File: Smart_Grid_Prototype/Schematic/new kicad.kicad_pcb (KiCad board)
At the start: 2 copper layers, 144.8 x 116.8 mm, 70 parts, among them J1 EXT_POW, J2 24VAC _LOAD, J3 AC_INPUT, J4 DC_LOAD, J5 POW_SHARE, Q1 BD139, Q2 BD139, Q3 BD139, Q4 BD139, Q5 BD139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

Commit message: updated
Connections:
- U1 pad 15: unconnected-(U1-VIN-Pad15) -> /EXT_POWER
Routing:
- net /EXT_POWER: track 114.2 -> 161.9 mm
- net GND: track 452.7 -> 467.4 mm
- removed copper zone on B.Cu, net GND
- removed copper zone on F.Cu, net GND

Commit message: Perfect PCB
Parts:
- added J6: USB_C_Receptacle_PowerOnly_6P, Connector_USB:USB_C_Receptacle_GCT_USB4125-xx-x-0190_6P_TopMnt_Horizontal, F.Cu at (149.2, 152.2)
- added R32: 5.1k, Resistor_THT:R_Axial_DIN0207_L6.3mm_D2.5mm_P15.24mm_Horizontal, F.Cu at (177.3, 145.2)
- added R33: 5.1k, Resistor_THT:R_Axial_DIN0207_L6.3mm_D2.5mm_P15.24mm_Horizontal, F.Cu at (177.3, 149.2)
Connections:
- net /EXT_POWER renamed VCC
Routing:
- net GND: track 467.4 -> 612.4 mm, vias 4 -> 24
- net Net-(J6-CC1): track 0.00 -> 60.3 mm
- net Net-(J6-CC2): track 0.00 -> 29.6 mm
- net VCC: track 161.9 -> 185.7 mm
- added copper zone on B.Cu, net GND
- added copper zone on F.Cu, net GND
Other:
- board size 144.8 x 116.8 mm -> 153 x 119.8 mm

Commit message: perfect
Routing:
- net GND: track 612.4 -> 600.1 mm
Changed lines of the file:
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@@
+	)
+	(segment
+		(start 153.49 149.12)
+		(end 153.57 149.2)
+		(width 1.3)
+		(layer "F.Cu")
+		(net 1)
 	)
 	(segment
@@
 		(start 143.866346 144.78)
 		(end 134.62 144.78)
+		(width 1.3)
+		(layer "F.Cu")
+		(net 1)
+	)
+	(segment
+		(start 152 149.12)
+		(end 153.49 149.12)
 		(width 1.3)
 		(layer "F.Cu")
@@
 	)
 	(segment
-		(start 152 149.12)
-		(end 153.49 149.12)
-		(width 1.3)
-		(layer "F.Cu")
-		(net 1)
-	)
-	(segment
-		(start 146.5 149.12)
-		(end 145.01 149.12)
-		(width 0.8)
-		(layer "F.Cu")
-		(net 1)
-	)
-	(segment
-		(start 153.49 149.12)
-		(end 153.57 149.2)
-		(width 1.3)
-		(layer "F.Cu")
-		(net 1)
-	)
-	(segment
 		(start 205.83 93.89)
 		(end 208.28 91.44)
@@
 	)
 	(segment
+		(start 146.42 149.2)
+		(end 146.5 149.12)
+		(width 0.8)
+		(layer "F.Cu")
+		(net 1)
+	)
+	(segment
 		(start 186.55137 106.68)
 		(end 190.5 110.62863)
@@
 		(net 1)
 	)
+	(segment
+		(start 144.93 149.2)
+		(end 146.42 149.2)
+		(width 0.8)
+		(layer "F.Cu")
+		(net 1)
+	)
 	(via
 		(at 107.75 68.25)
@@
 	)
 	(segment
-		(start 144.93 153)
-		(end 153.57 153)
-		(width 1.3)
-		(layer "B.Cu")
-		(net 1)
-	)
-	(segment
 		(start 78.74 137.16)
 		(end 86.36 137.16)
@@
 		(width 1.3)
 		(layer "B.Cu")
-		(net 1)
-	)
-	(segment
-		(start 153.57 153)
-		(end 153.57 149.2)
-		(width 1.3)
-		(layer "B.Cu")

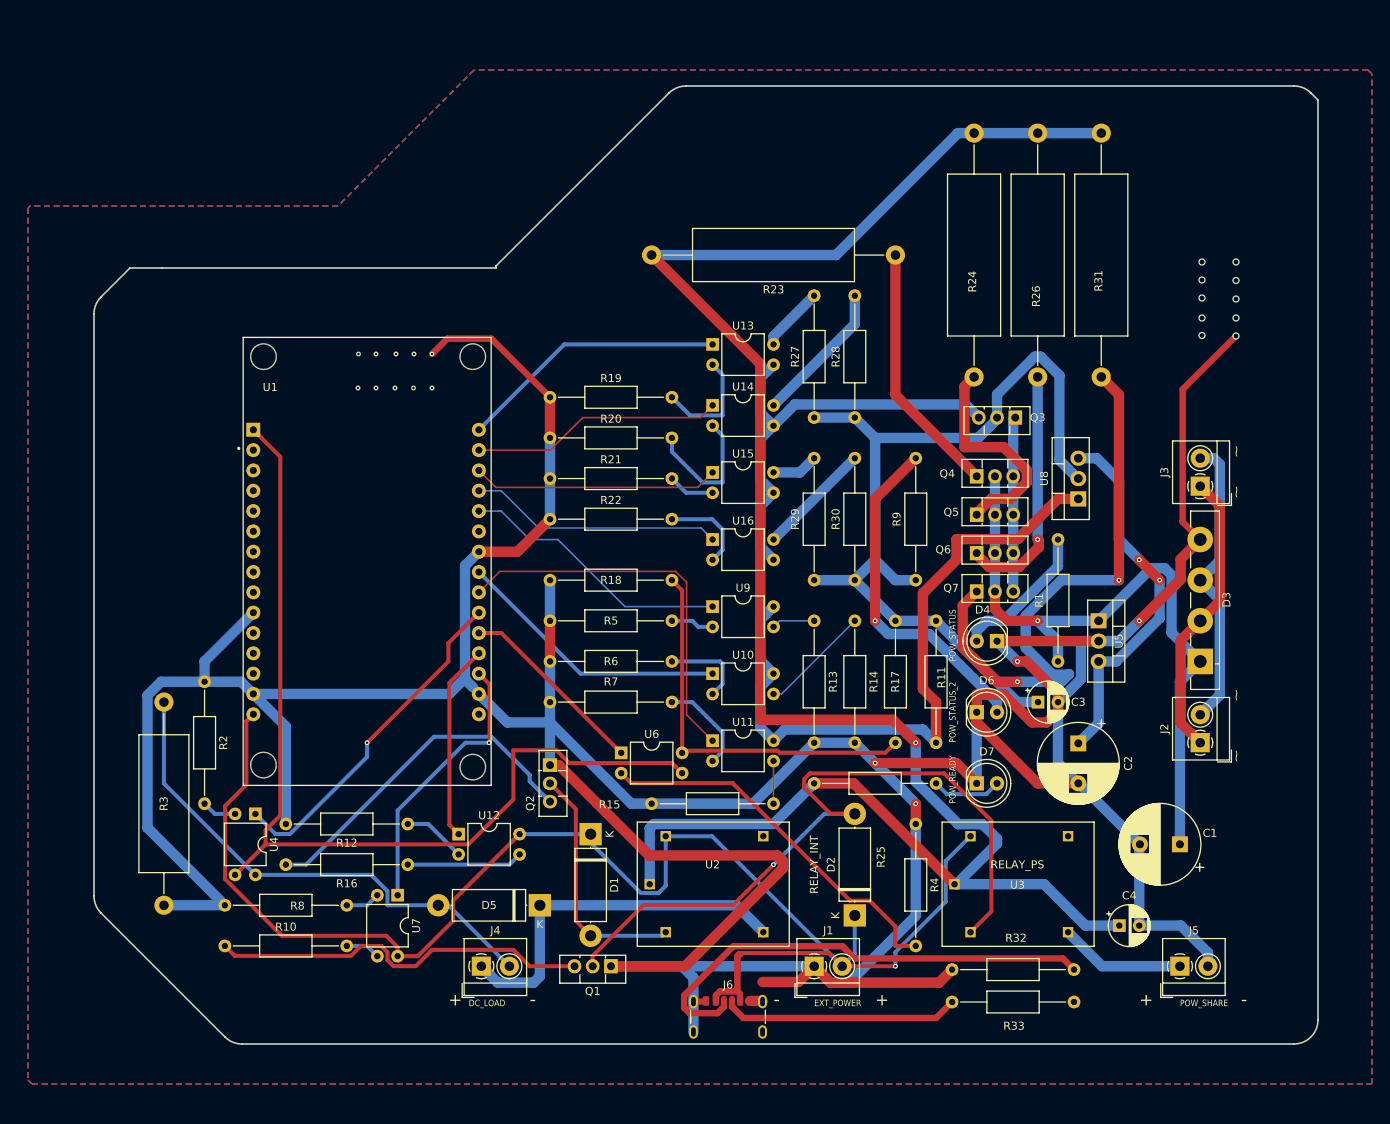
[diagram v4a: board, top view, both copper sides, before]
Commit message: ac load switch added
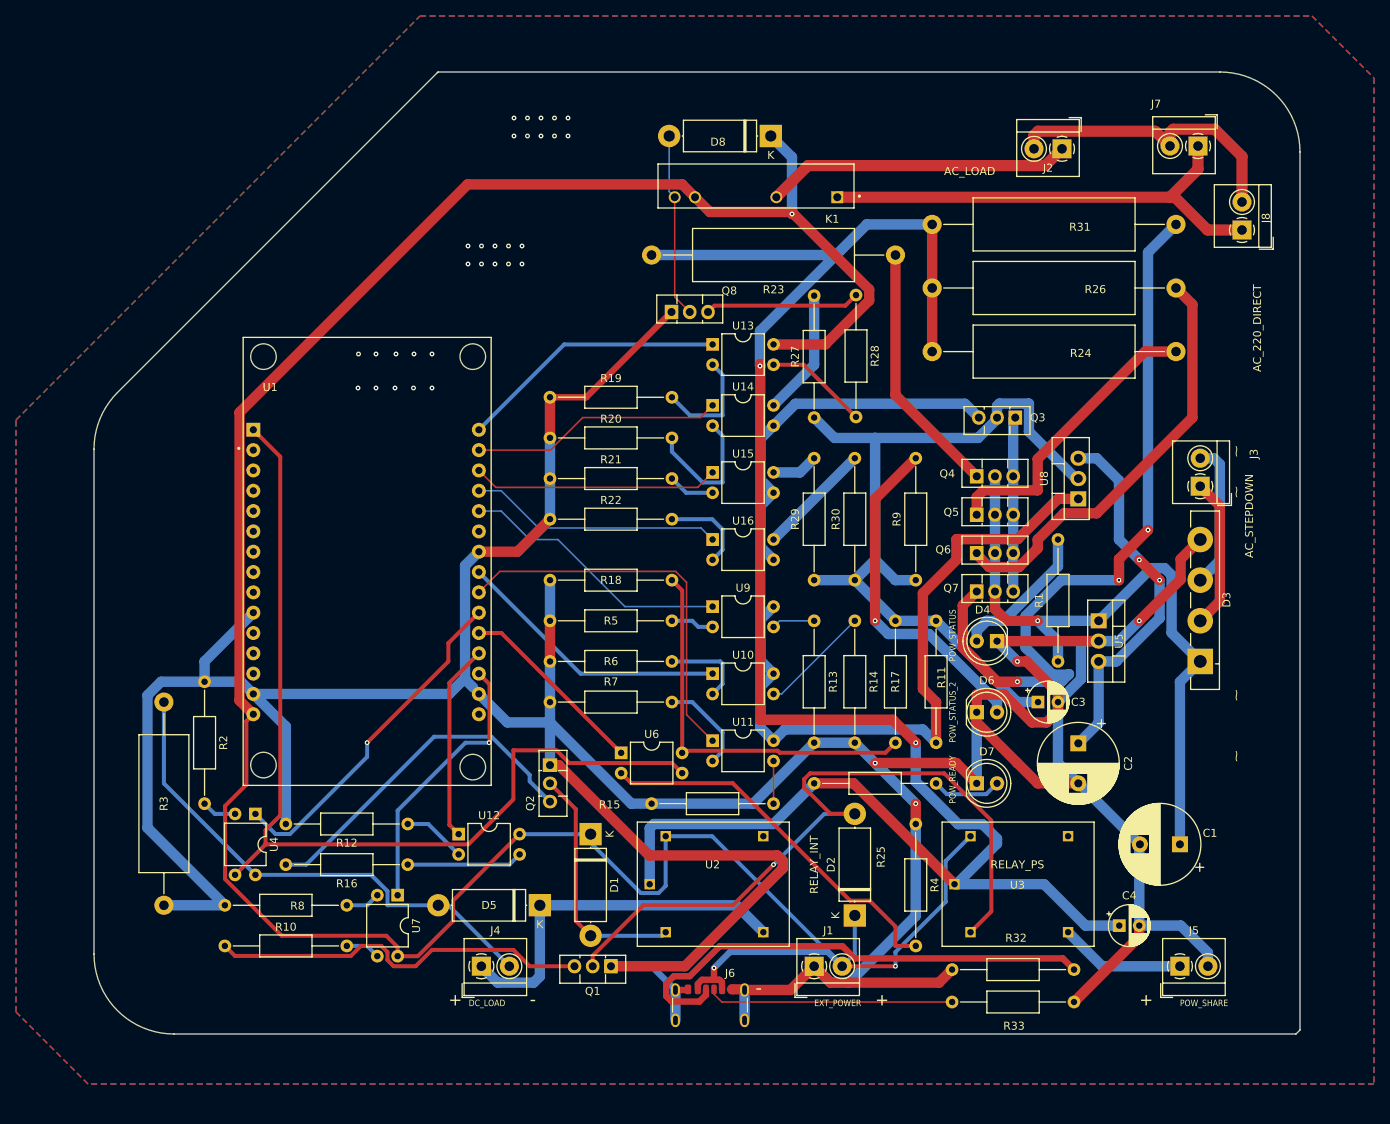
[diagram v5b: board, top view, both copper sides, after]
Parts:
- added D8: 1N5408/DIODE, Diode_THT:D_5W_P12.70mm_Horizontal, F.Cu at (154.6, 41.0)
- added J7: 220VAC, TerminalBlock_4Ucon:TerminalBlock_4Ucon_1x02_P3.50mm_Horizontal, F.Cu at (208.0, 42.2)
- added J8: 220VAC-TRANS, TerminalBlock_4Ucon:TerminalBlock_4Ucon_1x02_P3.50mm_Horizontal, F.Cu at (213.5, 52.8)
- added K1: G3MB-202PDC5, Library:RELAY_G3MB-202PDC5, F.Cu at (152.8, 47.2)
- added Q8: BD139, Package_TO_SOT_THT:TO-126-3_Vertical, F.Cu at (142.2, 63.0)
- J2: value 24VAC _LOAD -> AC_LOAD
- J3: value AC_INPUT -> AC_STEPDOWN
- R19: value 220 -> 220R
- R28: value 1k -> 120R
- moved J2 76.2 mm to (191.0, 42.6), turned to 180 degrees
- moved R24 25.4 mm to (205.2, 68.0), turned to 180 degrees
- moved R31 21.2 mm to (205.2, 52.0), turned to 180 degrees
- moved R26 20.6 mm to (205.2, 60.0), turned to 180 degrees
- moved R28 15.3 mm to (165.2, 60.9), turned to -90 degrees
- moved J6 2.68 mm to (147.0, 150.8)
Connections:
- D3 pad 2: Net-(J2-Pin_1) -> Net-(J3-Pin_1)
- J2 pad 1: Net-(J2-Pin_1) -> /ACL+
- J2 pad 2: VAC -> /AC-
- J3 pad 1: Net-(J2-Pin_1) -> Net-(J3-Pin_1)
- R28 pad 1: /V_OUT -> Net-(Q8-B)
- R28 pad 2: /1k_R -> Net-(R28-Pad2)
- U13 pad 3: /CURRENT_CONTROL -> Net-(R28-Pad2)
- U13 pad 4: /150_R -> VCC
- U14 pad 4: /1k_R -> /150_R
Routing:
- net VCC: track 185.7 -> 347.2 mm, vias 1 -> 3
- net /AC+: track 0.00 -> 60.1 mm
- net /ACL+: track 0.00 -> 38.2 mm
- net /AC-: track 0.00 -> 37.6 mm
- net Net-(J2-Pin_1): track 36.1 -> 0.00 mm
- net GND: track 600.1 -> 570.3 mm, vias 24 -> 34
- net /RELAY_AC: track 0.00 -> 23.1 mm
- net /E3_TO_R: track 31.2 -> 53.4 mm, vias 1 -> 0
- net /E4_TO_R: track 73.8 -> 94.9 mm, vias 2 -> 3
- net Net-(Q8-B): track 0.00 -> 19.4 mm
- net VAC: track 37.1 -> 18.3 mm
- net Net-(J3-Pin_1): track 0.00 -> 18.8 mm
- net /1k_R: track 17.9 -> 0.00 mm
- net Net-(R28-Pad2): track 0.00 -> 13.0 mm
- net /LOAD+: track 248.0 -> 236.7 mm, vias 1 -> 2
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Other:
- board size 153 x 119.8 mm -> 150.8 x 120.2 mm
- board text added: "AC_220_DIRECT"
- board text added: "AC_LOAD"
- board text added: "AC_STEPDOWN"

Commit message: minor changes
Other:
- board size 150.8 x 120.2 mm -> 148.5 x 117.3 mm
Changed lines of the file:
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@@
 	)
 	(gr_line
-		(start 113 33)
-		(end 210.75 33)
-		(stroke
-			(width 0.05)
-			(type default)
-		)
-		(layer "Edge.Cuts")
-	)
-	(gr_line
-		(start 220.75 152.75)
-		(end 220.25 153.25)
+		(start 110 36)
+		(end 212.375 36)
 		(stroke
 			(width 0.05)
@@
 	)
 	(gr_line
-		(start 220.25 153.25)
-		(end 80 153.25)
+		(start 215 36)
+		(end 213.75 36)
 		(stroke
 			(width 0.05)
@@
 		(layer "Edge.Cuts")
 	)
-	(gr_arc
-		(start 210.75 33)
-		(mid 217.821068 35.928932)
-		(end 220.75 43)
+	(gr_line
+		(start 80 153.25)
+		(end 208.5 153.25)
 		(stroke
 			(width 0.05)
@@
 	(gr_line
 		(start 72.928932 73.071068)
-		(end 112.919951 33.080049)
+		(end 110.001031 35.998969)
+		(stroke
+			(width 0.05)
+			(type default)
+		)
+		(layer "Edge.Cuts")
+	)
+	(gr_arc
+		(start 218.5 143.25)
+		(mid 215.571068 150.321068)
+		(end 208.5 153.25)
 		(stroke
 			(width 0.05)
@@
 	)
 	(gr_line
-		(start 220.75 43)
-		(end 220.75 152.75)
+		(start 218.5 143.25)
+		(end 218.5 43.642136)
 		(stroke
 			(width 0.05)
@@
 	)
 	(gr_line
-		(start 112.919951 33.080049)
-		(end 113 33)
+		(start 213.75 36)
+		(end 212.375 36)
 		(stroke
 			(width 0.05)
@@
 		(layer "Edge.Cuts")
 	)
+	(gr_line
+		(start 215.571068 36.571068)
+		(end 215 36)
+		(stroke
+			(width 0.05)
+			(type default)
+		)
+		(layer "Edge.Cuts")
+	)
+	(gr_arc
+		(start 215.571068 36.571068)
+		(mid 217.738784 39.815304)
+		(end 218.5 43.642136)
+		(stroke
+			(width 0.05)
+			(type default)
+		)
+		(layer "Edge.Cuts")
+	)
 	(gr_text "SMART GRID PROTOTYPE"
 		(at 101.03 68.35 90)
@@
 		(polygon
 			(pts
-				(xy 230 159.5) (xy 69.25 159.5) (xy 60.25 150.5) (xy 60.25 76.5) (xy 110.75 26) (xy 222.25 26) (xy 230 33.75)
+				(xy 63.25 31.75) (xy 63.25 144.75) (xy 81 162.5) (xy 220.25 162.5) (xy 226 156.75) (xy 226 35.25)
+				(xy 222.5 31.75)
 			)
 		)
